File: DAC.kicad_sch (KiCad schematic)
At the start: 0 parts

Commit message: Adding official files from course download
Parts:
- added C400: 10u, Capacitor_SMD:C_0603_1608Metric, symbol Device:C
- added C401, C406: 100n, Capacitor_SMD:C_0402_1005Metric, symbol Device:C
- added C402: 1u, Capacitor_SMD:C_0603_1608Metric, symbol Device:C
- added C403, C405: 1n, Capacitor_SMD:C_0402_1005Metric, symbol Device:C
- added C404: 150p, Capacitor_SMD:C_0402_1005Metric, symbol Device:C
- added D400: PESD3V3L1BA,115, Diode_SMD:D_SOD-323, symbol Device:D_TVS
- added J400: 031-5640-1010, PhilsLab_Footprints_KiCad6:AMPHENOL-BNC-031-5640-1010, symbol Connector:Conn_Coaxial
- added R400: 0R, Resistor_SMD:R_0402_1005Metric, symbol Device:R
- added R401: 10k, Resistor_SMD:R_0402_1005Metric, symbol Device:R
- added R402: 6k8, Resistor_SMD:R_0402_1005Metric, symbol Device:R
- added R403: 22k, Resistor_SMD:R_0402_1005Metric, symbol Device:R
- added R404: 12k, Resistor_SMD:R_0402_1005Metric, symbol Device:R
- added R405: 49R9, Resistor_SMD:R_0402_1005Metric, symbol Device:R
- added U400: DAC7563SDGSR, PhilsLab_Footprints_KiCad6:VSSOP-10, symbol PhilsLab-KiCad-Symbols:DAC7563SDGSR
- added U401: MCP6001T-E/OT, Package_TO_SOT_SMD:SOT-23-5, symbol Amplifier_Operational:MCP6001-OT
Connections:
- new net: C403.1, R402.1, R403.2
- new net: C405.1, R403.1, R404.2
- new net +3.3VA: C406.1, U401.5 (V+)
- new net +3V3: C400.1, C401.1, U400.9 (AVDD)
- new net DAC_NCLR: U400.5 (NCLR)
- new net DAC_NLDAC: U400.4 (NLDAC)
- new net DAC_OUT_A: R402.2, U400.1 (VOUT_A)
- new net DAC_OUT_B: R401.1, U400.2 (VOUT_B)
- new net DAC_SCLK: R400.2, U400.7 (SCLK)
- new net DAC_VREF: C402.1, U400.10 (VREFIN/VREFOUT)
- new net GND: C400.2, C401.2, C402.2, C403.2, C404.2, C406.2, D400.2 (A2), J400.2 (Ext), R401.2, U400.3 (GND), U401.2 (V-)
- new net OUT: D400.1 (A1), J400.1 (In), R405.1
- new net OUT_AA_BUF_IN: C404.1, R404.1, U401.3 (+)
- new net OUT_AA_BUF_OUT: C405.2, R405.2, U401.1, U401.4 (-)
- new net SPI2_MOSI: U400.8 (DIN)
- new net SPI2_NSS: U400.6 (NSYNC)
- new net SPI2_SCK: R400.1
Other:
- note added: "3rd order Butterworth anti-aliasing (low-pass filter) fc=25kHz"
- note added: "Anti-Aliasing Filter and Output Connector (BNC)"
- note added: "C(Vref,min)=150nF"
- note added: "DAC"
- note added: "DC offset (op-amp bias) generated by DAC"
- note added: "Output voltage will be in 0V to +3.3V range!"
- note added: "Rout=50R"
- note added: "[4] DAC & Analogue Output Circuitry"
- company: (none) -> Phil's Lab
- title: (none) -> Mixed-Signal Demo PCB

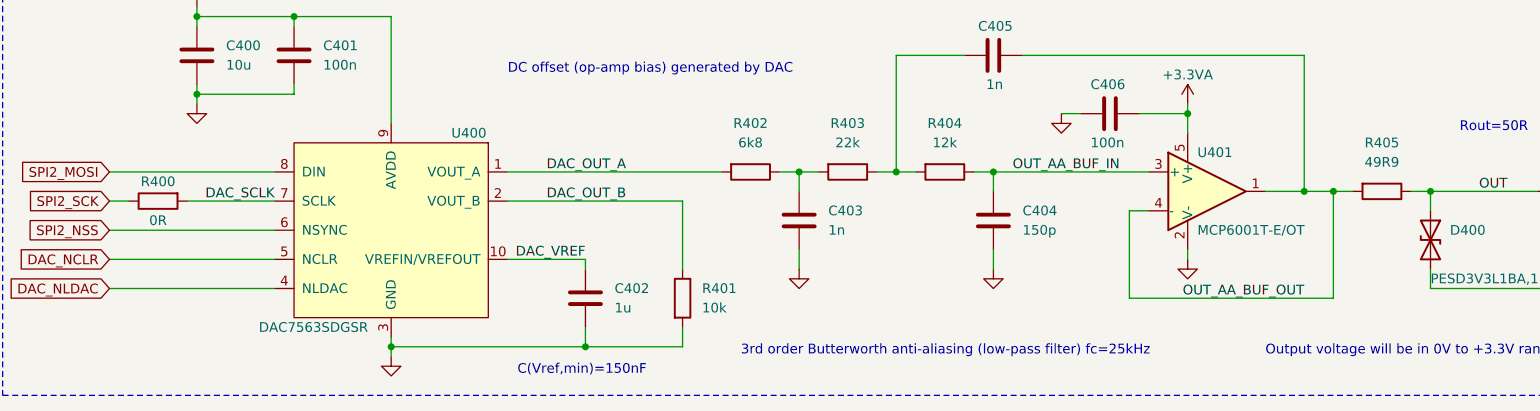
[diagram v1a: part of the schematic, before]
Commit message: Add backup file and updates to schematic
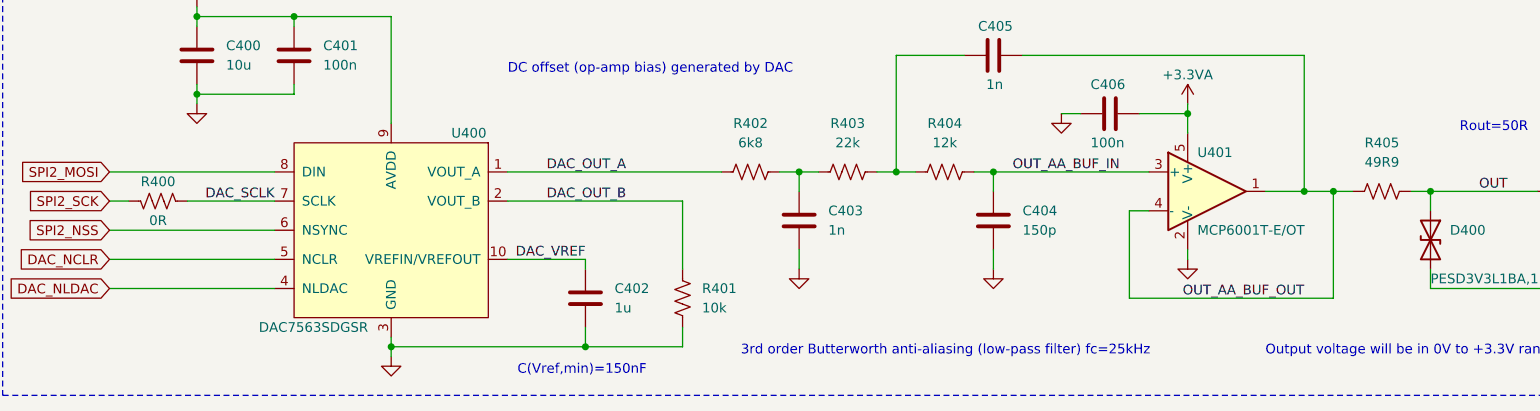
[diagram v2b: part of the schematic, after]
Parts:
- R400, R401, R402, R403, R404, R405: symbol Device:R -> Device:R_US
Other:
- company: Phil's Lab -> Jacob Parent
- title: Mixed-Signal Demo PCB -> Mixed-Signal PCB
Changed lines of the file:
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@@
 	(paper "A4")
 	(title_block
-		(title "Mixed-Signal Demo PCB")
+		(title "Mixed-Signal PCB")
+		(date "6-1-2024")
 		(rev "0.1")
-		(company "Phil's Lab")
+		(company "Jacob Parent")
 	)
 	(junction
@@
 	)
 	(symbol
-		(lib_id "Device:R")
+		(lib_id "Device:R_US")
 		(at 58.42 96.52 90)
 		(mirror x)
@@
 		)
 		(property "Footprint" "Resistor_SMD:R_0402_1005Metric"
-			(at 58.42 94.742 90)
+			(at 58.674 97.536 90)
 			(effects
 				(font
@@
 			)
 		)
-		(property "Description" ""
+		(property "Description" "Resistor, US symbol"
 			(at 58.42 96.52 0)
 			(effects
@@
 	)
 	(symbol
-		(lib_id "Device:R")
+		(lib_id "Device:R_US")
 		(at 127 109.22 0)
 		(unit 1)
@@
 		)
 		(property "Footprint" "Resistor_SMD:R_0402_1005Metric"
-			(at 125.222 109.22 90)
+			(at 128.016 109.474 90)
 			(effects
 				(font
@@
 			)
 		)
-		(property "Description" ""
+		(property "Description" "Resistor, US symbol"
 			(at 127 109.22 0)
 			(effects
@@
 	)
 	(symbol
-		(lib_id "Device:R")
+		(lib_id "Device:R_US")
 		(at 135.89 92.71 270)
 		(unit 1)
@@
 		)
 		(property "Footprint" "Resistor_SMD:R_0402_1005Metric"
-			(at 135.89 90.932 90)
+			(at 135.636 93.726 90)
 			(effects
 				(font
@@
 			)
 		)
-		(property "Description" ""
+		(property "Description" "Resistor, US symbol"
 			(at 135.89 92.71 0)
 			(effects
@@
 	)
 	(symbol
-		(lib_id "Device:R")
+		(lib_id "Device:R_US")
 		(at 148.59 92.71 270)
 		(unit 1)
@@
 		)
 		(property "Footprint" "Resistor_SMD:R_0402_1005Metric"
-			(at 148.59 90.932 90)
+			(at 148.336 93.726 90)
 			(effects
 				(font
@@
 			)
 		)
-		(property "Description" ""
+		(property "Description" "Resistor, US symbol"
 			(at 148.59 92.71 0)
 			(effects
@@
 	)
 	(symbol
-		(lib_id "Device:R")
+		(lib_id "Device:R_US")
 		(at 161.29 92.71 270)
 		(unit 1)
@@
 		)
 		(property "Footprint" "Resistor_SMD:R_0402_1005Metric"
-			(at 161.29 90.932 90)
+			(at 161.036 93.726 90)
 			(effects
 				(font
@@
 			)
 		)
-		(property "Description" ""
+		(property "Description" "Resistor, US symbol"
 			(at 161.29 92.71 0)
 			(effects
@@
 	)
 	(symbol
-		(lib_id "Device:R")
+		(lib_id "Device:R_US")
 		(at 218.44 95.25 270)
 		(unit 1)
@@
 		)
 		(property "Footprint" "Resistor_SMD:R_0402_1005Metric"
-			(at 218.44 93.472 90)
+			(at 218.186 96.266 90)
 			(effects
 				(font
@@
 			)
 		)
-		(property "Description" ""
+		(property "Description" "Resistor, US symbol"
 			(at 218.44 95.25 0)
 			(effects

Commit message: Add files via upload
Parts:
- J400: footprint PhilsLab_Footprints_KiCad6:AMPHENOL-BNC-031-5640-1010 -> MixedSignalBoardParts:BNC
- U400: footprint PhilsLab_Footprints_KiCad6:VSSOP-10 -> MixedSignalBoardParts:SOIC-10
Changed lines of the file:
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@@
 			)
 		)
-		(property "Footprint" "PhilsLab_Footprints_KiCad6:VSSOP-10"
+		(property "Footprint" "MixedSignalBoardParts:SOIC-10"
 			(at 88.9 105.41 0)
 			(effects
@@
 			)
 		)
-		(property "Footprint" "PhilsLab_Footprints_KiCad6:AMPHENOL-BNC-031-5640-1010"
+		(property "Footprint" "MixedSignalBoardParts:BNC"
 			(at 243.84 95.25 0)
 			(effects
@@
 			)
 		)
-		(property "Datasheet" " ~"
+		(property "Datasheet" "~"
 			(at 243.84 95.25 0)
 			(effects
